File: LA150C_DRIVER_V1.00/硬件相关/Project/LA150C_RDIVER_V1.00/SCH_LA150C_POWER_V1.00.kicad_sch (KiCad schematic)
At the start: 21 parts, among them Q1 PMOS, U5 SCT2230MLUAR

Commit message: chore: save LA150C schematic updates
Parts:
- removed C1: 47uF, symbol Device:C
- removed C2: 100nF, symbol Device:C
- removed C4: 10uF, Capacitors:C1210, symbol LA150C_RDIVER_V1.00:GRM32EC72A106KE05L
- removed C5: 100nF, Capacitors:C_0402_1005Metric, symbol LA150C_RDIVER_V1.00:GRM155R71H104KE14D
- removed Q1: PMOS, symbol Transistor_FET:Q_PMOS_GSD
- removed R1: 10K, Resistors:R0201, symbol LA150C_RDIVER_V1.00:RC0201FR-0710KL
- added C1, C2, C3, C7, C8: 1uF, Capacitors:C0603, symbol Capacitors:GRM188D72A105KE01D
- renumbered C7 to C4, C8 to C5, C9 to C6, C6 to C9, R4 to R1, R3 to R2, R5 to R3, R9 to R4, R8 to R5, R10 to R6, R6 to R7, R7 to R8, U5 to U1
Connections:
- net VBUS_IN is gone; now on net VBUS: D1.2 (A2)
- net PGND: now also C1.2, C2.2, C3.2, C7.2, C8.2
- net VBUS: now also C1.1, C2.1, C3.1, C7.1, C8.1
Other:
- moved on the sheet: C10, C4, C5, C6, D1, R1, R3, R7, R8

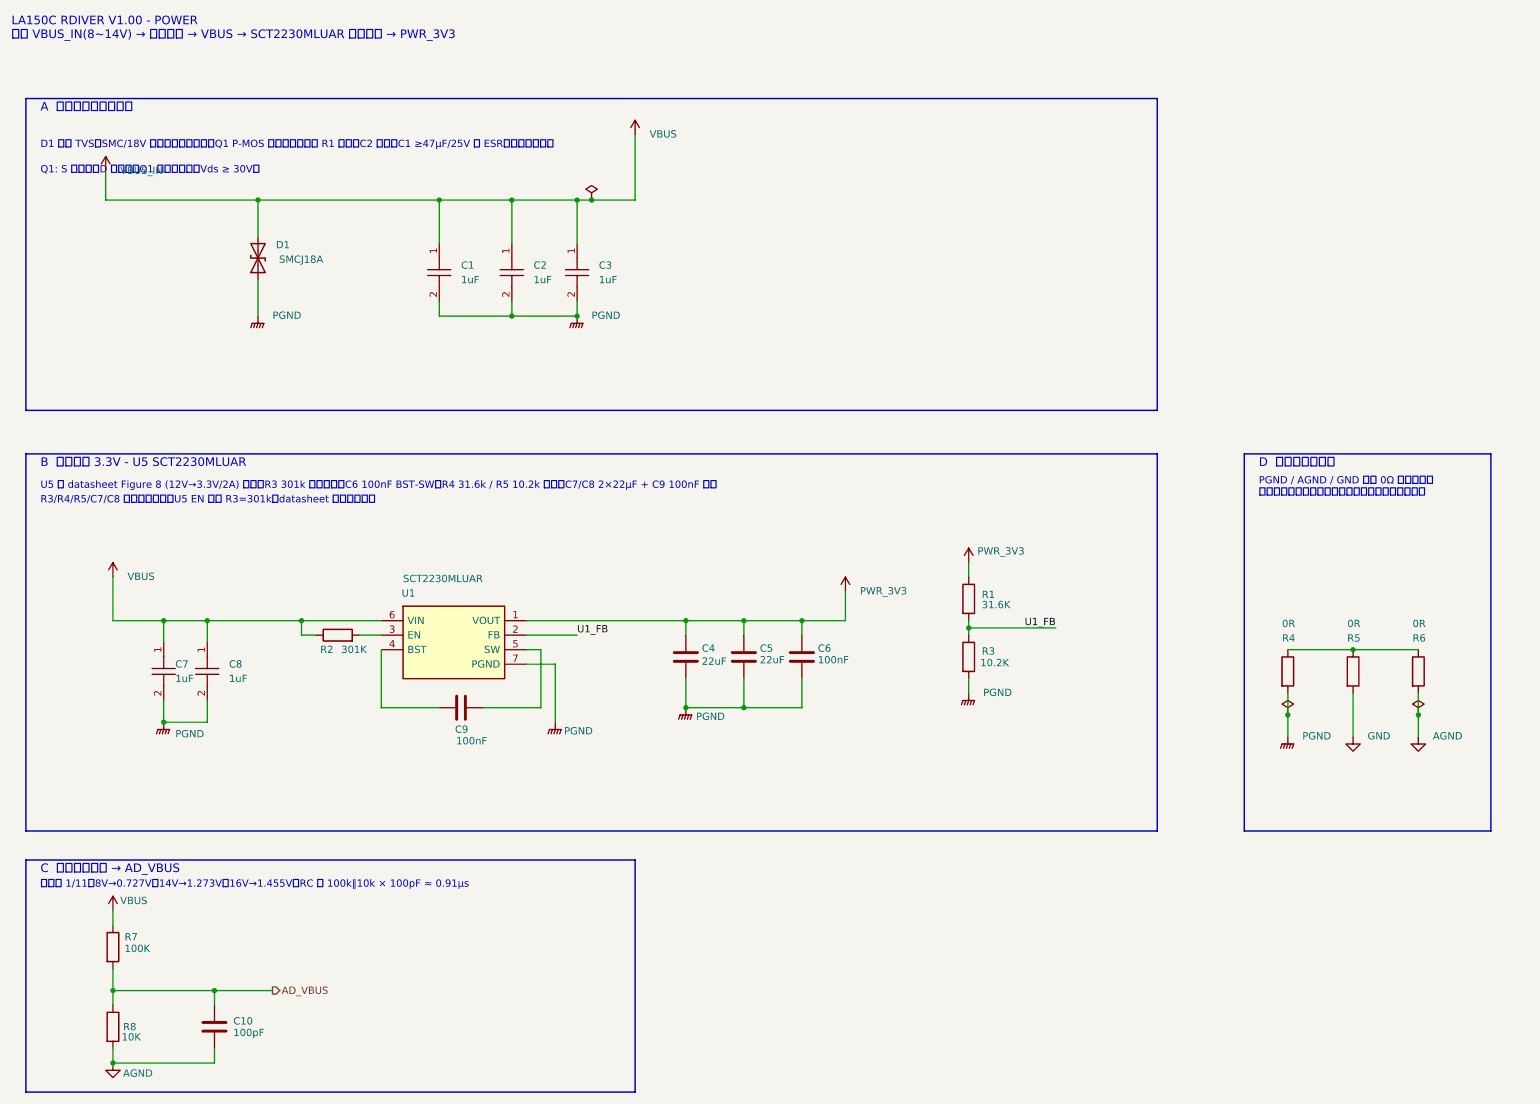
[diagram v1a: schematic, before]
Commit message: feat: finalize LA150C driver schematic
Align the GD32F503 BGA64 pin resources with QS01 V1.12, retain the SCT2230, MT6701 and CAN FD circuits, replace the motor test points with 1.0 x 2.0 mm solder pads, and update the symbols, footprints, ERC report, netlist, BOM and PDF.
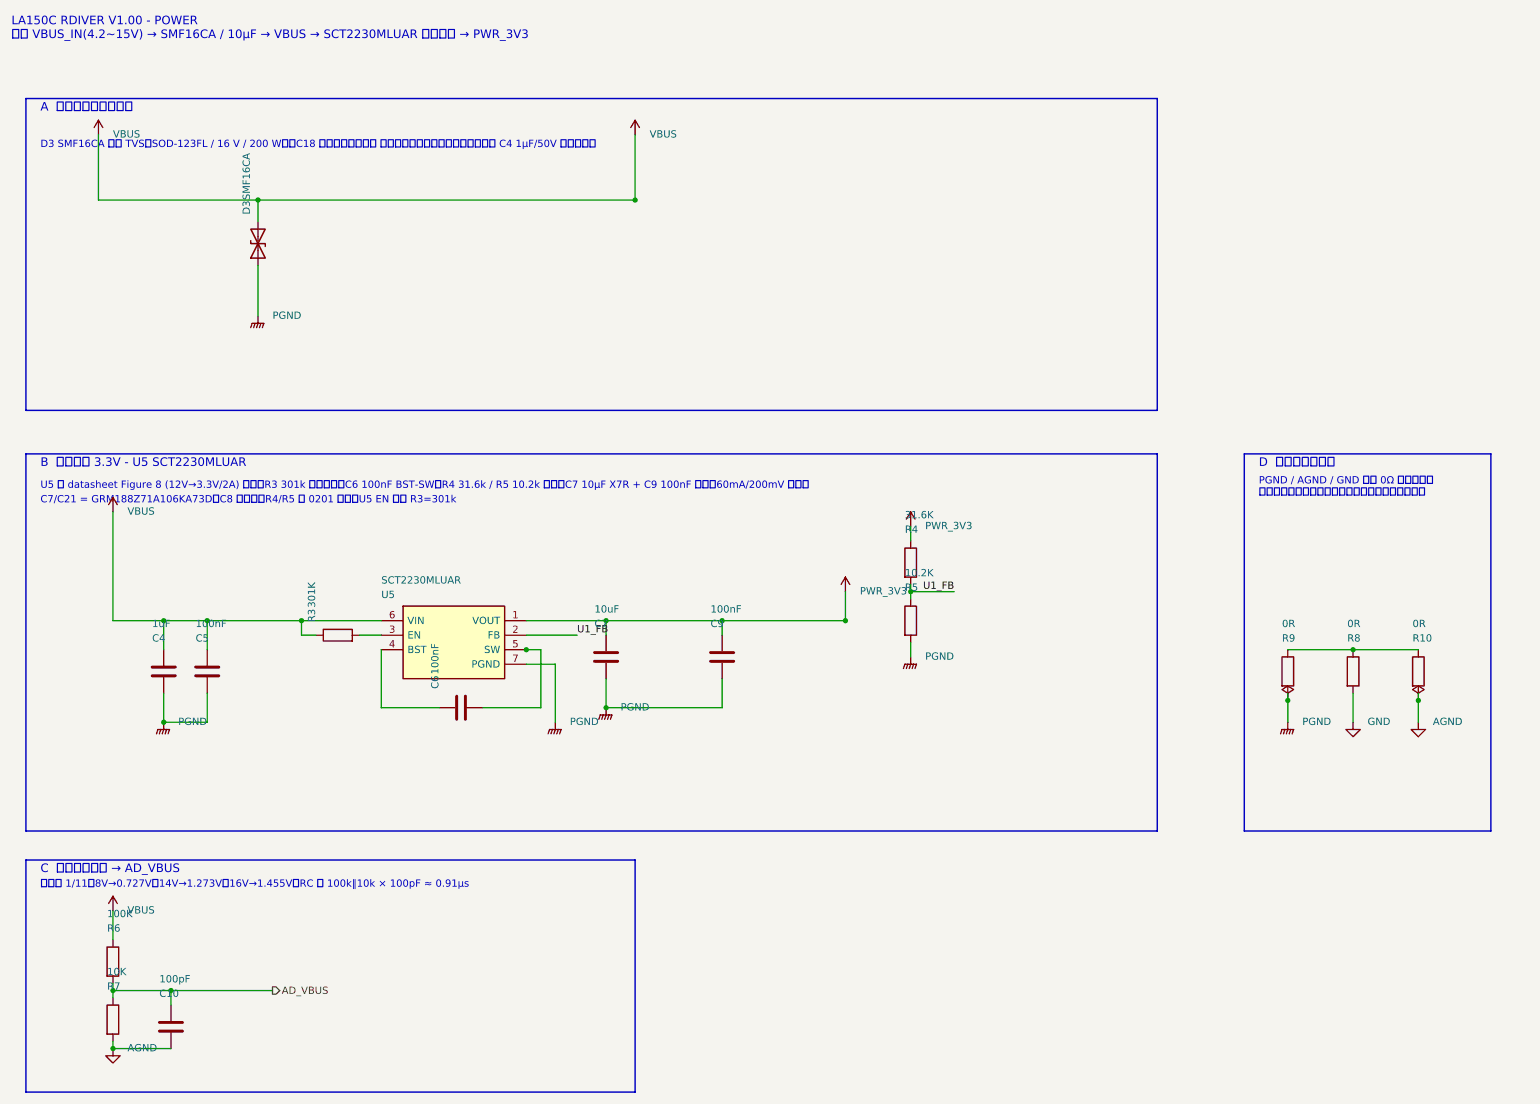
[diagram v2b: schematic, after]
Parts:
- removed C1, C2, C3, C7, C8: 1uF, Capacitors:C0603, symbol Capacitors:GRM188D72A105KE01D
- removed C5: 22uF, symbol Device:C
- removed D1: SMCJ18A, symbol Device:D_TVS
- added C4: 1uF, Capacitors:C_0603_1608Metric, symbol LA150C_RDIVER_V1.00:CL10B105KB8NQNC
- added C5: 100nF, Capacitors:C_0402_1005Metric, symbol LA150C_RDIVER_V1.00:GRM155R71H104KE14D
- added D3: SMF16CA, Circuit Protection:D_SOD-123F, symbol LA150C_RDIVER_V1.00:SMF16CA
- C10: footprint Capacitors:C_0201_0603Metric -> Capacitors:C0201; symbol LA150C_RDIVER_V1.00:FN03N100J500PLG -> LA150C_RDIVER_V1.00:CL03C101JB3NNNC; LCSC Part C561710 -> C730413; MPN FN03N100J500PLG -> CL03C101JB3NNNC; Manufacturer PSA -> Samsung Electro-Mechanics
- C7: renamed from C4; value 22uF -> 10uF; footprint (none) -> Capacitors:C_0603_1608Metric; symbol Device:C -> LA150C_RDIVER_V1.00:GRM188Z71A106KA73D; LCSC Part (none) -> C2959727; MPN (none) -> GRM188Z71A106KA73D; Manufacturer (none) -> muRata(村田)
- R10: renamed from R6; Manufacturer YAGEO(国巨) -> YAGEO
- R4: renamed from R1; footprint (none) -> Resistors:R_0201_0603Metric
- R5: renamed from R3; footprint (none) -> Resistors:R_0201_0603Metric
- R6: renamed from R7; Manufacturer YAGEO(国巨) -> YAGEO
- R7: renamed from R8; Manufacturer YAGEO(国巨) -> YAGEO
- R8: renamed from R5; Manufacturer YAGEO(国巨) -> YAGEO
- R9: renamed from R4; Manufacturer YAGEO(国巨) -> YAGEO
- renumbered C9 to C6, C6 to C9, R2 to R3, U1 to U5
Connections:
- net PGND: now also C4.2, C5.2, D3.1 (A1)
- net VBUS: now also C4.1, C5.1, D3.2 (A2)
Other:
- note added: "C7/C21 = GRM188Z71A106KA73D；C8 已删除；R4/R5 改 0201 封装；U5 EN 分压 R3=301k"
- note added: "D3 SMF16CA 双向 TVS（SOD-123FL / 16 V / 200 W）；C18 按空间优化删除， 母线储能由控制板承担，驱动板保留 C4 1µF/50V 本地旁路。"
- note added: "LA150C RDIVER V1.00 - POWER 母线 VBUS_IN(4.2~15V) → SMF16CA / 10µF → VBUS → SCT2230MLUAR 同步降压 → PWR_3V3"
- note added: "U5 按 datasheet Figure 8 (12V→3.3V/2A) 配置：R3 301k 使能分压、C6 100nF BST-SW、R4 31.6k / R5 10.2k 反馈、C7 10µF X7R + C9 100nF 输出（60mA/200mV 目标）"
- note removed: "D1 母线 TVS（SMC/18V 档，型号待确认）；Q1 P-MOS 反接保护，栅极 R1 下拉、C2 去抖；C1 ≥47µF/25V 低 ESR（料号待确认）"
- note removed: "LA150C RDIVER V1.00 - POWER 母线 VBUS_IN(8~14V) → 反接保护 → VBUS → SCT2230MLUAR 同步降压 → PWR_3V3"
- note removed: "Q1: S 接输入，D 接输出；Q1 型号待确认（Vds ≥ 30V）"
- note removed: "R3/R4/R5/C7/C8 暂无确认料号；U5 EN 分压 R3=301k（datasheet 典型应用值）"
- note removed: "U5 按 datasheet Figure 8 (12V→3.3V/2A) 配置：R3 301k 使能分压、C6 100nF BST-SW、R4 31.6k / R5 10.2k 反馈、C7/C8 2×22µF + C9 100nF 输出"
- moved on the sheet: C10, C7, C9, R4, R5, R6, R7
